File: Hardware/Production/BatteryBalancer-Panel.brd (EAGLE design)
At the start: 118.5 x 117.3 mm, 478 parts, among them IC1 OP-AMP, IC2 OP-AMP, IC3 OP-AMP, IC4 OP-AMP, IC5 OP-AMP, J2 ISP, J3 ISP, J5 ISP, J7 ISP, J9 ISP, U1 TAP_POINT, U10 MCP1755, U11 AD7280A, U12 ATMEGA328P_TQFP, U13 CH340C, U14 TAP_POINT, U15 TAP_POINT, U16 TAP_POINT, U17 TAP_POINT, U18 MCP1755, U19 AD7280A, U2 TAP_POINT, U20 CH340C, U21 ATMEGA328P_TQFP, U22 TAP_POINT, U23 TAP_POINT, U24 TAP_POINT, U25 TAP_POINT, U26 TAP_POINT, U27 MCP1755, U28 AD7280A, U29 CH340C, U3 TAP_POINT, U30 ATMEGA328P_TQFP, U31 TAP_POINT, U32 TAP_POINT, U33 TAP_POINT, U34 TAP_POINT, U35 TAP_POINT, U36 MCP1755, U37 AD7280A, U38 CH340C, U39 ATMEGA328P_TQFP, U4 TAP_POINT, U40 TAP_POINT, U41 TAP_POINT, U42 TAP_POINT, U43 TAP_POINT, U44 TAP_POINT, U45 MCP1755, U5 TAP_POINT, U6 AD7280A, U7 CH340C, U8 ATMEGA328P_TQFP, U9 TAP_POINT, Y1 16MHz, Y2 16MHz, Y3 16MHz, Y4 16MHz, Y5 16MHz

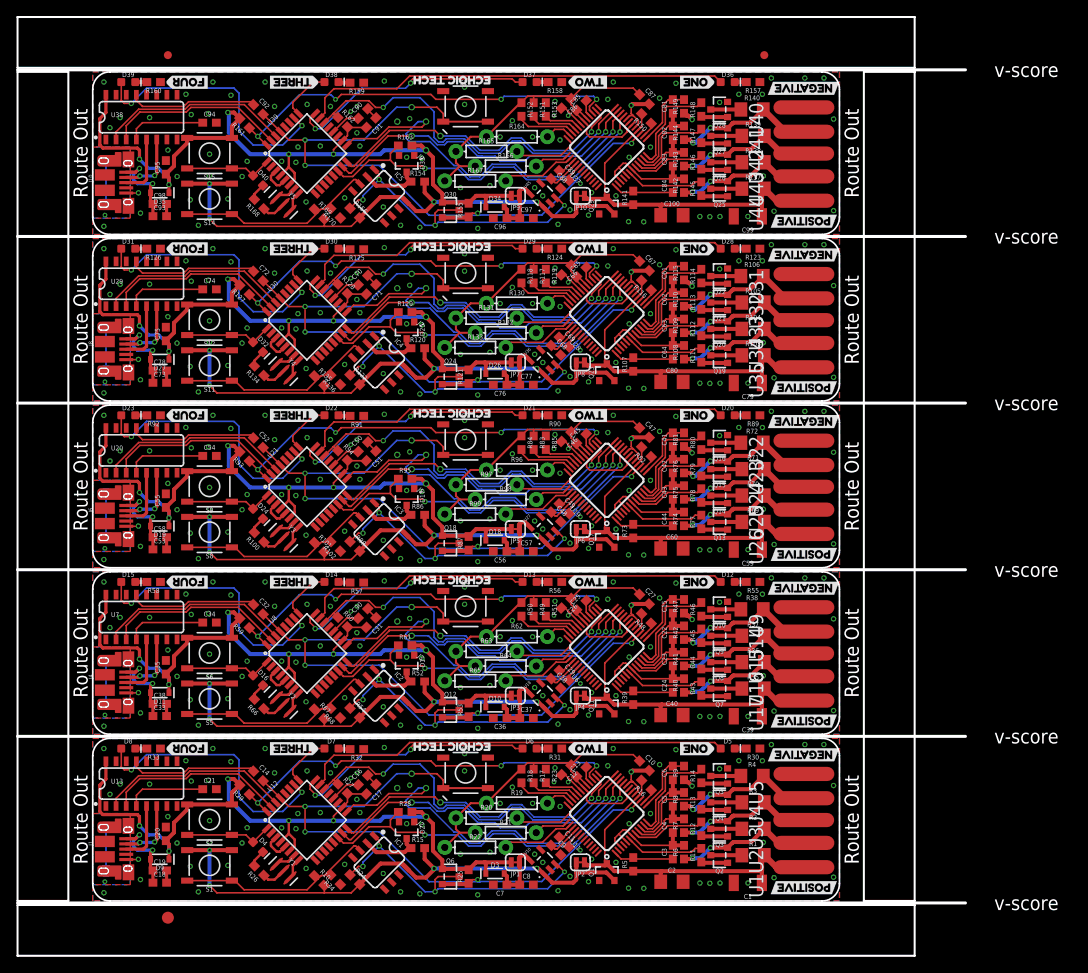
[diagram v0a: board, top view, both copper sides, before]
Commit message: Increase manufacturability, re panelize + CAM
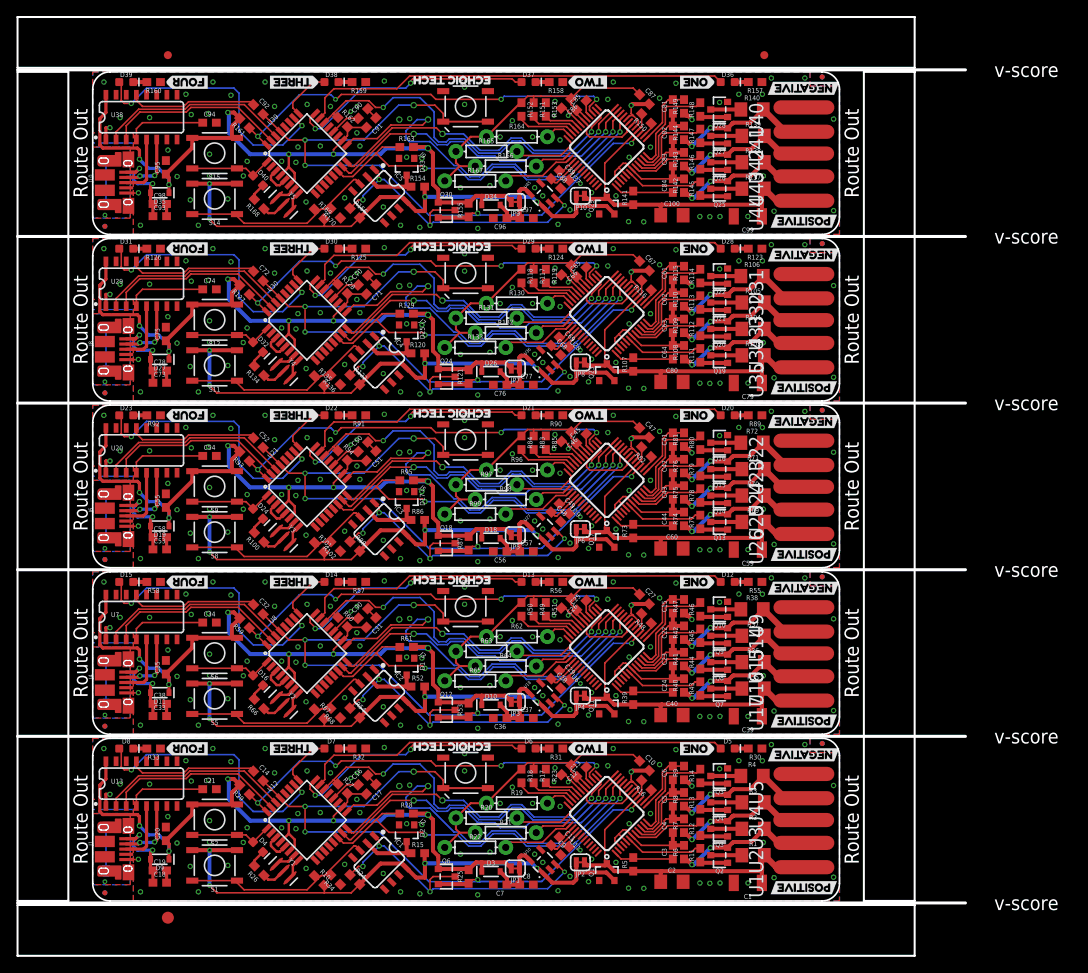
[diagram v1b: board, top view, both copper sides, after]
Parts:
- added FD1, FD10, FD11, FD12, FD13, FD14, FD15, FD16, FD17, FD18, FD19, FD2, FD20, FD3, FD4, FD5, FD6, FD7, FD8, FD9: FIDUCIALUFIDUCIAL, SparkFun-Aesthetics:FIDUCIAL-MICRO
- moved JP3 0.76 mm to (52.8, 24.9)
- moved JP5 0.76 mm to (52.8, 45.7)
- moved JP7 0.76 mm to (52.8, 66.5)
- moved JP9 0.76 mm to (52.8, 87.4)
- moved JP1 0.76 mm to (52.8, 4.06)
- moved R15 0.63 mm to (40.6, 5.97)
- moved S1 0.63 mm to (15.2, 4.45)
- moved S11 0.63 mm to (15.2, 66.9)
- moved S12 0.63 mm to (15.2, 72.6)
- moved S14 0.63 mm to (15.2, 87.8)
- moved S15 0.63 mm to (15.2, 93.5)
- moved S2 0.63 mm to (15.2, 10.2)
- moved S5 0.63 mm to (15.2, 25.3)
- moved S6 0.63 mm to (15.2, 31.0)
- moved S8 0.63 mm to (15.2, 46.1)
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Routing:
- net GND4: track 26.8 -> 28.8 mm, vias 86 -> 84
- net GND3: track 26.8 -> 28.8 mm, vias 86 -> 84
- net GND1: track 26.8 -> 28.8 mm, vias 86 -> 84
- net GND2: track 26.8 -> 28.8 mm, vias 86 -> 84
- net GND: track 26.8 -> 28.8 mm, vias 86 -> 84
- net !CS3: track 45.6 -> 47.3 mm
- net !CS4: track 45.6 -> 47.3 mm
- net !CS2: track 45.6 -> 47.3 mm
- net !CS1: track 45.6 -> 47.3 mm
- net !CS: track 45.6 -> 47.3 mm
- net VCC2: track 97.6 -> 99.1 mm
- net VCC: track 97.6 -> 99.1 mm
- net VCC4: track 97.6 -> 99.1 mm
- net VCC3: track 97.6 -> 99.1 mm
- net VCC1: track 97.6 -> 99.1 mm
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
